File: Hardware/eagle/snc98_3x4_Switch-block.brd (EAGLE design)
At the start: 56.4 x 83.2 mm, 73 parts

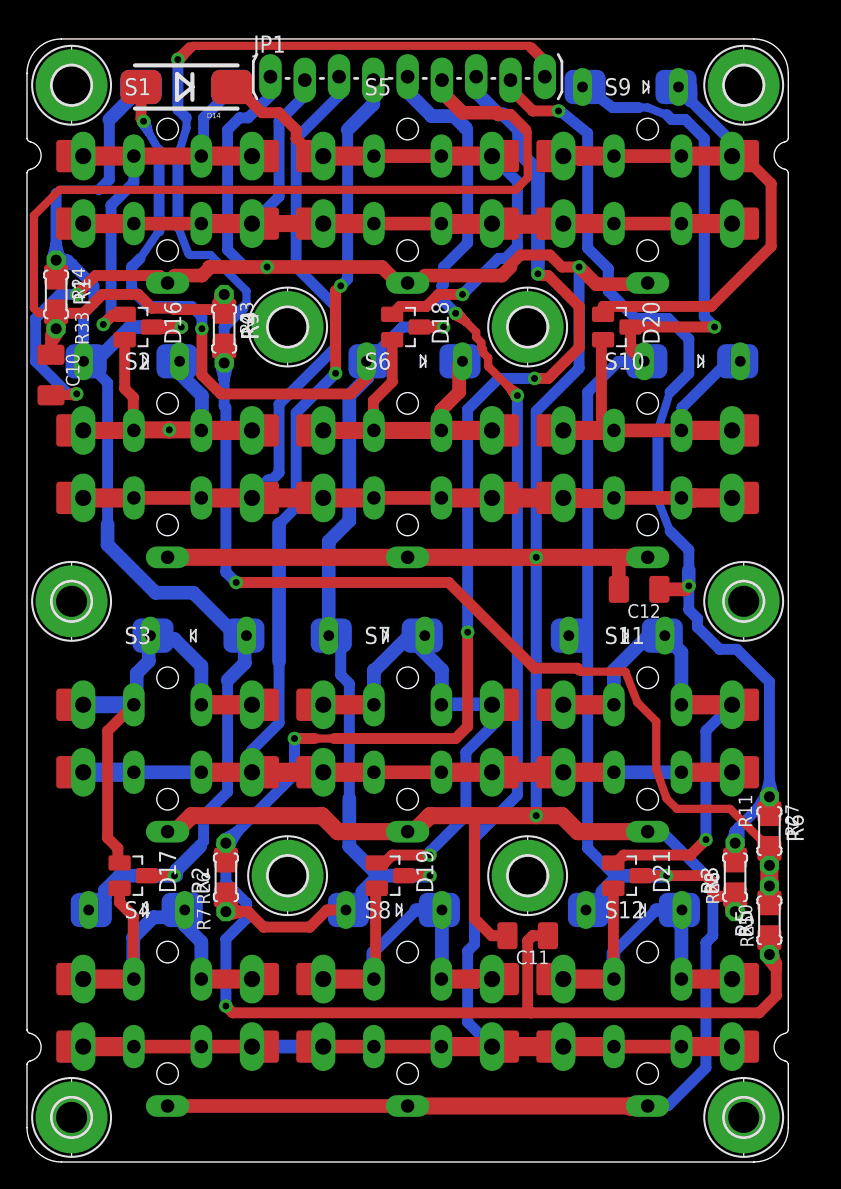
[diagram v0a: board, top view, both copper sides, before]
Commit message: change_to_6mm_taktile_switch
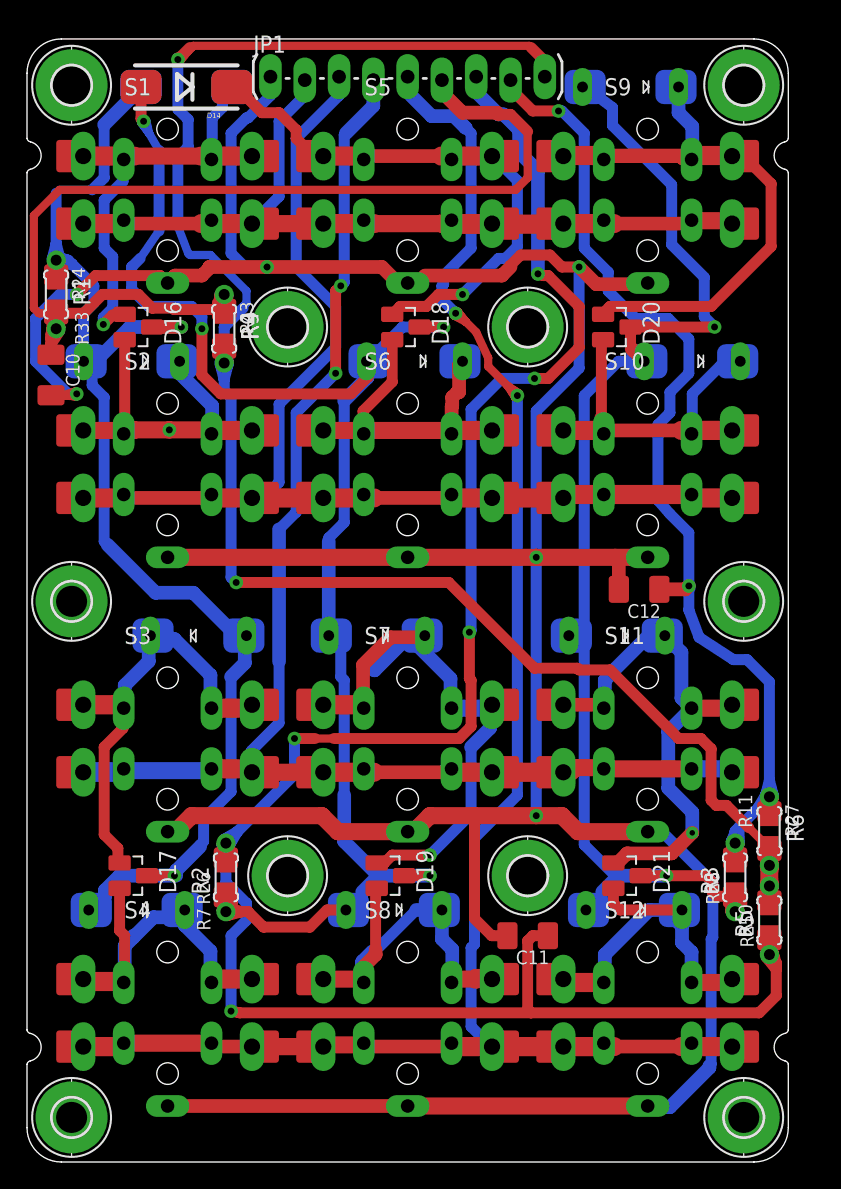
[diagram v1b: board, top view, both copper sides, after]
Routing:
- net C4: track 141.8 -> 163.8 mm
- net C3: track 106.6 -> 125.0 mm
- net N$16: track 45.9 -> 53.2 mm
- net N$28: track 40.2 -> 47.4 mm
- net N$25: track 29.1 -> 34.4 mm
- net N$6: track 35.6 -> 39.1 mm
- net A_3: track 100.6 -> 98.1 mm
- net C2: track 88.0 -> 90.3 mm
- net N$2: track 30.1 -> 32.4 mm
- net C1: track 67.3 -> 69.1 mm
- net N$24: track 41.6 -> 43.1 mm
- net N$18: track 28.9 -> 30.1 mm
- net AREF: track 177.4 -> 178.5 mm
- net N$30: track 30.6 -> 31.6 mm
- net N$19: track 28.6 -> 29.5 mm
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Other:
- board text added: "snc98 3x4 Switch-block Rev. 0.5"
- board text removed: "snc98 3x4 Switch-block Rev. 0.4"

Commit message: cbrt_int96
cbrt added
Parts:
- removed D1, D2, D29, D3, D4, D5: SD103CW, BaseApp:SMADIODE-WIDE
- removed D6, D7, D8: SD103C, BaseApp:280MIL-TH
- added D01, D02, D03, D04, D05, D06, D07, D08, D09: SD103AW-DIO, BaseApp:SOD-123F
- D10, D11, D12: device BaseApp:SMADIODE-WIDE -> BaseApp:SOD-123F
- D13, D14, D15: value SD103CW -> BAT54A; device BaseApp:SMADIODE-WIDE -> diode:SOT23
- D19, D20, D21: value BAT54A -> SD103C; device diode:SOT23 -> BaseApp:280MIL-TH
- moved D14 58.6 mm to (7.87, 21.2), turned to 270 degrees
- moved D12 55.1 mm to (45.0, 18.7)
- moved D17 54.2 mm to (43.7, 61.8)
- moved D25 44.8 mm to (44.7, 79.6)
- moved D16 44.7 mm to (26.9, 21.2)
- moved D18 43.8 mm to (44.5, 21.2)
- moved D19 42.7 mm to (7.75, 59.3), turned to 0 degrees
- moved D27 41.3 mm to (43.7, 39.0)
- moved D22 40.7 mm to (28.7, 59.3)
- moved D20 38.5 mm to (12.7, 39.0), turned to 180 degrees
- moved D21 36.4 mm to (8.13, 18.7), turned to 0 degrees
- moved D23 27.0 mm to (25.9, 39.0)
- moved D11 25.2 mm to (43.7, 39.0)
- moved D24 25.0 mm to (27.2, 18.7), turned to 0 degrees
- moved D15 24.3 mm to (28.1, 61.8), flipped to the top, turned to 270 degrees
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- renumbered D9 to D28
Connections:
- net A_1: now also D01.A, D02.A, D03.A, D04.A, D13.3, D14.3, D19.P$1, D20.P$1, D21.P$1; no longer D1.A, D12.A, D13.A, D16.3, D17.3, D23.P$1, D24.P$1, D27.P$1, D29.A
- net A_2: now also D05.A, D06.A, D07.A, D08.A, D15.3, D16.3, D23.P$1, D24.P$1; no longer D11.A, D14.A, D18.3, D19.3, D2.A, D25.P$1, D26.P$1, D5.A
- net A_3: now also D09.A, D11.A, D12.A, D17.3, D18.3, D25.P$1, D26.P$1, D27.P$1; no longer D15.A, D20.3, D21.3, D3.A, D4.A, D6.P$1, D7.P$1, D8.P$1
- net N$16: now also D09.C, D17.1, D25.P$2; no longer D15.C, D20.1, D6.P$2
- net N$18: now also D17.2, D26.P$2; no longer D20.2, D7.P$2
- net N$19: now also D02.C, D13.2, D19.P$2; no longer D12.C, D16.2, D27.P$2
- net N$2: now also D04.C, D14.2, D21.P$2; no longer D1.C, D17.2, D23.P$2
- net N$21: now also D11.C, D18.1, D27.P$2; no longer D21.1, D4.C, D8.P$2
- net N$22: now also D12.C, D18.2; no longer D21.2, D3.C
- net N$24: now also D05.C, D15.1; no longer D14.C, D18.1
- net N$25: now also D06.C, D15.2, D22.P$2; no longer D11.C, D18.2, D26.P$2
- net N$28: now also D07.C, D16.1, D23.P$2; no longer D19.1, D25.P$2, D5.C
- net N$30: now also D08.C, D16.2, D24.P$2; no longer D19.2, D2.C, D22.P$2
- net N$32: now also D03.C, D14.1, D20.P$2; no longer D17.1, D24.P$2, D29.C
- net N$6: now also D01.C, D13.1; no longer D13.C, D16.1
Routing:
- net A_1: track 113.1 -> 121.3 mm
- net A_2: track 125.0 -> 132.1 mm
- net A_3: track 98.1 -> 103.5 mm
- net AREF: track 178.5 -> 176.3 mm
- net N$24: track 43.1 -> 44.9 mm
- net N$16: track 53.2 -> 55.0 mm
- net N$19: track 29.5 -> 31.3 mm
- net N$28: track 47.4 -> 45.8 mm
- net N$18: track 30.1 -> 31.2 mm
- net N$25: track 34.4 -> 35.2 mm
- net N$21: track 40.4 -> 41.1 mm
- net N$32: track 36.4 -> 35.8 mm
- net N$30: track 31.6 -> 32.1 mm

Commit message: add factorial() - today from -72 to +72.
add factorial() - today from -72 to +72.
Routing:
- net A_2: track 132.1 -> 131.5 mm
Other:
- outline, holes or cut-outs redrawn
